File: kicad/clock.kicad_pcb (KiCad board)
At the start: 4 copper layers, 110 x 110 mm, 187 parts, among them J1 USB4160-03-0230-C, J10 Knob: EM14 enc+SW (top face), J11 Radio-off toggle (rear), J12 NeoPixel ext (5V/DATA/GND, po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, J2 PROG, J3 Speaker DMA58-4 (4R), J6 DM3AT-SF-PEJM5, J7 Sensor board (BME688+TSL2591+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, J9 Wake COB 12V (warm+cool), M1 X40.879, Q1 2N7002, Q2 AO3401A, Q3 2N7002, Q4 AO3401A, Q6 AO3400A, Q7 AO3400A, Q8 2N7002, Q9 AO3401A, SW1 RESET, SW2 BOOT, U1 CH224K, U10 LTC4412ES6, U11 TB6612FNG, U12 TB6612FNG, U13 MCP23017, U14 QRE1113GR, U15 SN74AHCT1G125, U16 USBLC6-2SC6, U2 LT3652EMSE, U3 HY2111-GB, U4 AOSD32334C, U5 TPS61023, U6 TLV62569DBVR, U7 TPS55340PWPR, U8 ESP32-S3-WROOM-1-N16R8, U9 TAS5760MDAPR, Y1 32.768kHz

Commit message: Move C238 next to U15 (#9)
The SN74AHCT1G125 buffer that drives the whole SK6812 chain had its bypass
capacitor 50.5 mm away, i.e. no local decoupling at all.

  C238 (76.50, 39.50) -> (26.73, 46.18) rot 180
  pad 1 (+5V) to U15 pin 5 (VCC):  50.50 -> 1.75 mm
  new 0.50 mm B.Cu trace, 2 GND vias 0.62 mm from its return pad
  (nearest GND via was 2.68 mm)

One subtlety worth recording: C238's +5V pad was not a leaf but a JUNCTION
between two collinear B.Cu tracks, (77.28,44.36)->pad and (77.28,33.61)->pad.
Cutting both, as the mover did at first, split +5V into two islands.  Tracks
that share an endpoint stay connected without the pad, so the rule is now to
cut only when the pad holds a single stub, and to leave junctions alone.

DRC 0 errors / 0 warnings / 0 unconnected; review_check.py 11/12, 0 regressions.

Co-Authored-By: Claude Opus 5 <noreply@anthropic.com>
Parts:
- moved C238 50.2 mm to (26.7, 46.2)
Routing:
- net +5V: track 265.3 -> 267.1 mm
- net GND: vias 477 -> 479
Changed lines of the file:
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@@
 	(footprint "Capacitor_SMD:C_0603_1608Metric"
 		(layer "B.Cu")
-		(at 76.5 39.5 180)
+		(at 26.73 46.18 180)
 		(descr "Capacitor SMD 0603 (1608 Metric), square (rectangular) end terminal, IPC-7351 nominal, (Body size source: IPC-SM-782 page 76, https://www.pcb-3d.com/wordpress/wp-content/uploads/ipc-sm-782a_amendment_1_and_2.pdf)")
 		(tags "capacitor")
@@
 	)
 	(via
+		(at 25.879664 46.800443)
+		(size 0.8)
+		(drill 0.4)
+		(layers "F.Cu" "B.Cu")
+		(net "GND")
+	)
+	(via
 		(at 56.925 41.925)
 		(size 0.6)
@@
 	)
 	(via
+		(at 26.58 46.18)
+		(size 0.6)
+		(drill 0.3)
+		(layers "F.Cu" "B.Cu")
+		(net "GND")
+	)
+	(via
 		(at 62.925 71.925)
 		(size 0.6)
@@
 		(layer "B.Cu")
 		(net "+5V")
+	)
+	(segment
+		(start 27.505 46.18)
+		(end 27.48 47.93)
+		(width 0.5)
+		(layer "B.Cu")
+		(net "+5V")

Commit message: Re-place and re-route the 32.768 kHz cluster (#24)
Item 1 of the #24 recommendation.  The load caps were 5.85 mm from Y1 and
their nets wandered 9.1 mm (XTAL_P) and 14.0 mm (XTAL_N) to reach them --
a large loop on MOhm-impedance nodes sitting near the switchers.

  C145 -> (58.90, 18.50)   pad 2 to Y1 pin 2:  5.85 -> 2.60 mm
  C146 -> (56.35, 22.11)   pad 2 to Y1 pin 1:  5.85 -> 1.75 mm
  XTAL_P copper   9.1 -> 5.46 mm   XTAL_N copper  14.0 -> 4.95 mm
  both nets on B.Cu only, 0 vias, as the recommendation asks
  4 GND vias ring the pair (0.62-1.52 mm from their return pads)

This could not be done as two independent part moves: the XTAL traces were
themselves counted as obstacles, yet they existed only to reach the caps'
old position, so nothing would fit next to Y1 until both nets were stripped
first.  It is one delete-place-reroute job.

Two tooling bugs it exposed, both now fixed:
  * courtyard collision was tested on BOUNDING BOXES.  U8's courtyard is a T
    (module body + antenna keep-out) whose bbox spans x[19.95,68.05]
    y[-13.79,27.50] and swallows the whole crystal corner, so every candidate
    near Y1 was rejected.  Now uses the real polygon.
  * a failed candidate restored the footprint ORIGIN to the PAD's coordinates,
    silently shifting both caps by the pad offset.

C145's first slot overlapped a hand-drawn 0.1 mm silk mark at (57.00,16.50)->
(58.50,18.00); C145 was nudged to clear it rather than moving the mark.
Reference fields for Y1/C145/C146/R113 were repositioned into the space the
caps vacated -- they had kept their old offsets and collided.

DRC 0 errors / 0 warnings / 0 unconnected; review_check.py 11/12, 0 regressions.

Co-Authored-By: Claude Opus 5 <noreply@anthropic.com>
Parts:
- moved C145 6.00 mm to (58.9, 18.5)
- moved C146 4.11 mm to (56.4, 22.1)
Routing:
- net Net-(U8-IO16_XTAL_N): track 14.0 -> 4.95 mm
- net Net-(U8-IO15_XTAL_P): track 9.06 -> 5.46 mm
- net GND: vias 479 -> 483
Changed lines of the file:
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@@
 	(footprint "Capacitor_SMD:C_0603_1608Metric"
 		(layer "B.Cu")
-		(at 55.905 26.2 180)
+		(at 56.35 22.115 180)
 		(descr "Capacitor SMD 0603 (1608 Metric), square (rectangular) end terminal, IPC-7351 nominal, (Body size source: IPC-SM-782 page 76, https://www.pcb-3d.com/wordpress/wp-content/uploads/ipc-sm-782a_amendment_1_and_2.pdf)")
 		(tags "capacitor")
 		(property "Reference" "C146"
-			(at -0.095 -1.8 0)
+			(at -0.1 -1.795 0)
 			(layer "B.SilkS")
 			(effects
@@
 		(tags "SMD SMT Crystal")
 		(property "Reference" "Y1"
-			(at 2.775 -0.4 0)
+			(at 6.185 0 0)
 			(layer "B.SilkS")
 			(effects
@@
 	(footprint "Capacitor_SMD:C_0603_1608Metric"
 		(layer "B.Cu")
-		(at 55.905 23.7 180)
+		(at 58.9 18.5 180)
 		(descr "Capacitor SMD 0603 (1608 Metric), square (rectangular) end terminal, IPC-7351 nominal, (Body size source: IPC-SM-782 page 76, https://www.pcb-3d.com/wordpress/wp-content/uploads/ipc-sm-782a_amendment_1_and_2.pdf)")
 		(tags "capacitor")
 		(property "Reference" "C145"
-			(at -2.595 -1.3 0)
+			(at -3.1 0 0)
 			(layer "B.SilkS")
 			(effects
@@
 		(tags "resistor")
 		(property "Reference" "R113"
-			(at -2.1682 -3.315 180)
+			(at -3.0682 0.485 180)
 			(layer "B.SilkS")
 			(effects
@@
 	)
 	(via
+		(at 60.22841 18.209548)
+		(size 0.8)
+		(drill 0.4)
+		(layers "F.Cu" "B.Cu")
+		(net "GND")
+	)
+	(via
 		(at 5.925 47.925)
 		(size 0.6)
@@
 	)
 	(via
+		(at 57.276194 21.354891)
+		(size 0.6)
+		(drill 0.3)
+		(layers "F.Cu" "B.Cu")
+		(net "GND")
+	)
+	(via
 		(at 32.925 38.925)
 		(size 0.6)
@@
 	)
 	(via
+		(at 61.014287 17.770662)
+		(size 0.8)
+		(drill 0.4)
+		(layers "F.Cu" "B.Cu")
+		(net "GND")
+	)
+	(via
 		(at 107.925 23.925)
 		(size 0.6)
@@
 	)
 	(via
+		(at 57.75 22.115)
+		(size 0.8)
+		(drill 0.4)
+		(layers "F.Cu" "B.Cu")
+		(net "GND")
+	)
+	(via
 		(at 26.925 83.925)
 		(size 0.6)
@@
 	)
 	(segment
-		(start 55.13 23.7)
-		(end 54.4496 23.0196)
-		(width 0.25)
-		(layer "B.Cu")
-		(net "Net-(U8-IO15_XTAL_P)")
-	)
-	(segment
-		(start 55.6 17.865)
-		(end 54.4496 17.865)
-		(width 0.25)
-		(layer "B.Cu")
-		(net "Net-(U8-IO15_XTAL_P)")
-	)
-	(segment
-		(start 54.4496 17.865)
-		(end 53.985 17.865)
-		(width 0.25)
-		(layer "B.Cu")
-		(net "Net-(U8-IO15_XTAL_P)")
-	)
-	(segment
-		(start 53.985 17.865)
-		(end 53.75 17.63)
+		(start 55.6 17.86)
+		(end 58.125 18.5)
 		(width 0.25)
 		(layer "B.Cu")
@@
 	(segment
 		(start 52.75 17.63)
-		(end 53.75 17.63)
-		(width 0.25)
-		(layer "B.Cu")
-		(net "Net-(U8-IO15_XTAL_P)")
-	)
-	(segment
-		(start 54.4496 23.0196)
-		(end 54.4496 17.865)
+		(end 55.6 17.865)
 		(width 0.25)
 		(layer "B.Cu")
@@
 	)
 	(segment
-		(start 52.75 18.9)
-		(end 53.75 18.9)
-		(width 0.25)
-		(layer "B.Cu")
-		(net "Net-(U8-IO16_XTAL_N)")
-	)
-	(segment
-		(start 55.8159 21.3309)
-		(end 55.8159 24.1907)
-		(width 0.25)
-		(layer "B.Cu")
-		(net "Net-(U8-IO16_XTAL_N)")
-	)
-	(segment
 		(start 55.6 20.365)
-		(end 55.6 21.115)
-		(width 0.25)
-		(layer "B.Cu")
-		(net "Net-(U8-IO16_XTAL_N)")
-	)
-	(segment
-		(start 55.6 21.115)
-		(end 55.8159 21.3309)
-		(width 0.25)
-		(layer "B.Cu")
-		(net "Net-(U8-IO16_XTAL_N)")
-	)
-	(segment
-		(start 55.5587 24.4479)
-		(end 55.5587 25.7713)
+		(end 55.575 22.115)
 		(width 0.25)
 		(layer "B.Cu")
@@
 	)
 	(segment
-		(start 54.7173 24.4479)
-		(end 53.75 23.4806)
-		(width 0.25)
-		(layer "B.Cu")
-		(net "Net-(U8-IO16_XTAL_N)")
-	)
-	(segment
-		(start 55.5587 25.7713)
-		(end 55.13 26.2)
-		(width 0.25)
-		(layer "B.Cu")
-		(net "Net-(U8-IO16_XTAL_N)")
-	)
-	(segment
-		(start 55.8159 24.1907)
-		(end 55.5587 24.4479)
-		(width 0.25)
-		(layer "B.Cu")
-		(net "Net-(U8-IO16_XTAL_N)")
-	)
-	(segment
-		(start 53.75 23.4806)
-		(end 53.75 18.9)
-		(width 0.25)
-		(layer "B.Cu")
-		(net "Net-(U8-IO16_XTAL_N)")
-	)
-	(segment
-		(start 55.5587 24.4479)
-		(end 54.7173 24.4479)
+		(start 52.75 18.9)
+		(end 55.6 20.365)
 		(width 0.25)
 		(layer "B.Cu")

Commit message: bom: MCU module N16R8 -> ESP32-S3-WROOM-1-N8R8
The 16 MB flash SKU was chosen back when the design carried the Sharp
display; it is also the harder variant to source. N8R8 is the DevKitC-1
stock variant, $6.32 / 1,709 in stock at DigiKey 15295891 (active) vs
$6.76 for the N16R8.

Verified drop-in against the WROOM-1/1U datasheet v1.8:

- Table 3-1 Pin Definitions is a single table for the whole series --
  41 pads, no per-SKU variation -- and the body stays 18.0 x 25.5 x
  3.1 mm, so the RF_Module:ESP32-S3-WROOM-1 land is unchanged.
- Note b reserves IO35/36/37 on any Octal-SPI-PSRAM module (ESP32-S3R8
  or R16V). N8R8 is R8, so the same 3 pads are eaten and the GPIO
  budget stays 32/33.
- R8 ambient range is unchanged at -40 ~ 65 C.
- Only the flash die differs: 16 MB -> 8 MB (Quad SPI).

Schematic/PCB changes are therefore text-only: MPN, Value and
Description on U8. No net, footprint or placement moved; ERC still
reports 0 violations and review_check.py is unchanged at 11/12 (the
U2 thermal-via TODO predates this). PCB copper untouched.

The one real cost is the partition table, reflowed for 8 MB in
FIRMWARE.md: OTA slots 3 M -> 2.5 M each, assets ~9 M -> ~2.7 M, with
coredump moved ahead of the app slots to keep ota_0 64 K-aligned at
0x40000. User tones were already microSD-only.

Also fixes the regen recipe in kicad/README.md, which omitted
stamp_bom.py -- without it build.py drops every BOM field from the
sheet.

Co-Authored-By: Claude Opus 5 <noreply@anthropic.com>
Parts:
- U8: value ESP32-S3-WROOM-1-N16R8 -> ESP32-S3-WROOM-1-N8R8
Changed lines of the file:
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@@
 			)
 		)
-		(property "Value" "ESP32-S3-WROOM-1-N16R8"
+		(property "Value" "ESP32-S3-WROOM-1-N8R8"
 			(at 0 -14.6 0)
 			(unlocked yes)
@@
 			)
 		)
-		(property "Description" "MODULE ESP32-S3 WIFI/BLE 16MB FLASH 8MB PSRAM"
+		(property "Description" "MODULE ESP32-S3 WIFI/BLE 8MB FLASH 8MB PSRAM"
 			(at 0 0 0)
 			(unlocked yes)
@@
 			)
 		)
-		(property "MPN" "ESP32-S3-WROOM-1-N16R8"
+		(property "MPN" "ESP32-S3-WROOM-1-N8R8"
 			(at 0 0 0)
 			(unlocked yes)

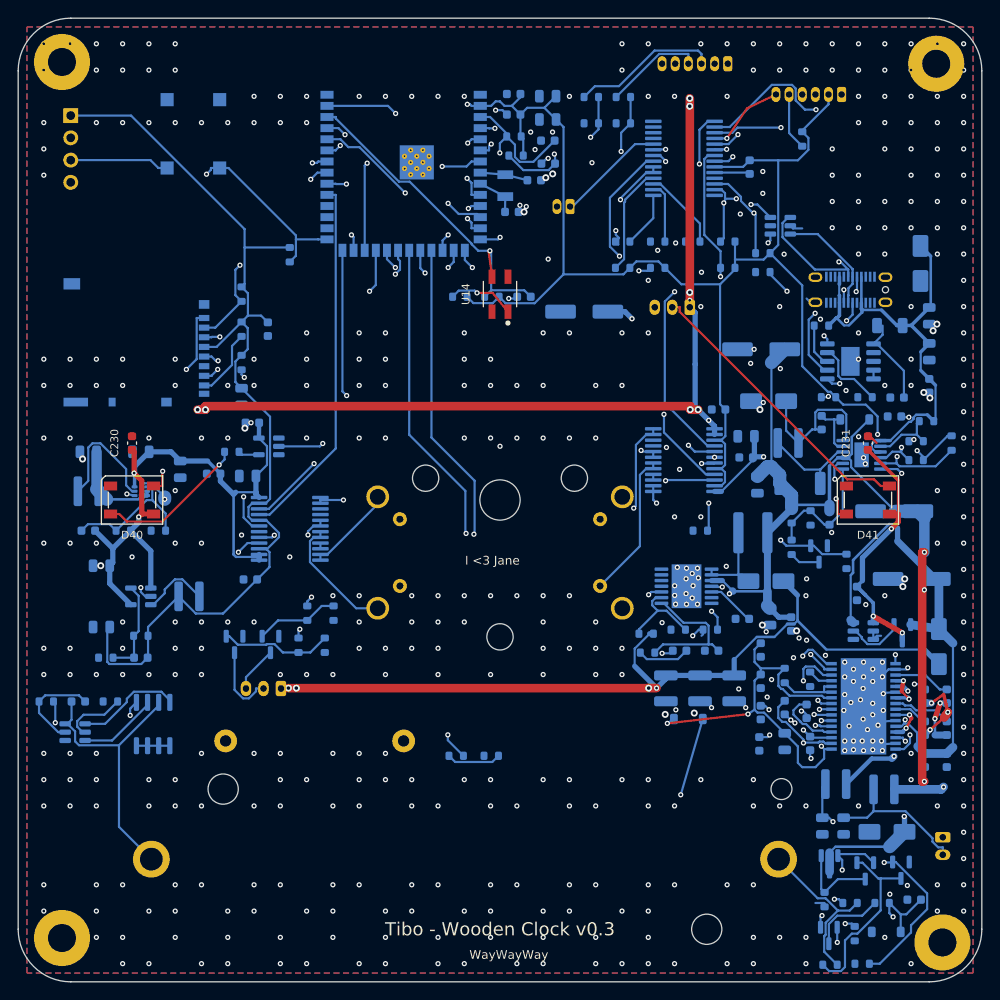
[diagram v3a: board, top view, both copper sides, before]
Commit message: pcb: pre-fab audit — R1 latent open (#26), +3V3 widths (#4), title block
Bundles the hand edits made in pcbnew (Y1 reference reposition, Q2 VBAT
stub re-route) with a pre-fab audit pass over the routed board looking
for defects that kicad-cli drc structurally cannot report.

#26 — R1 pad 2 was hanging on 0.049 mm of copper. A latent open left by
the #13 0603 -> 1206 land swap: the track ended at x = 98.675, dead
centre of the *old* 0603 pad, while the 1206 pad's outer edge sits at
98.600. Only the track's 0.125 mm end cap still overlapped. DRC was
silent because connectivity is a boolean -- any overlap reads as
connected. R1 feeds the CH224K's shunt-regulated VDD, so an open there
means no PD negotiation: no 15 V, no charging, no 12 V rail. Fixed with
one B.Cu segment to the pad centre, lying entirely inside the pad plus
the existing end cap, so no copper exists anywhere it did not already.

Sweeping the whole board for the same class found nothing else: 0 pads
and 0 free track ends now bridge on less than 0.12 mm (was 1 and 1,
both R1).

#4 — +3V3 widened in place. It was never in the POWER net class, so
a20faef skipped it and all 423 mm was still 0.25 mm, making it the
highest-resistance rail on the board. Width-only, no endpoint or part
moves, capped 0.80 mm outer / 0.60 mm inner:

    L3 -> U8 ESP32 3V3   258 -> 169 mOhm
    L3 -> U9 DVDD/AVDD   569/512 -> 393/346
    L3 -> U13 / U11 / J7 405/388/413 -> 273/270/285
    net total            837 -> 555 mOhm  (-34 %)

97 of 164 segments. Only the MCU figure has real consequences: DC droop
at a 500 mA Wi-Fi TX peak goes 129 -> 85 mV against 300 mV of margin to
the 3.0 V floor. Widening an inner-layer trace does not worsen #18 --
a slot's return-path cost is set by its length, not its width.

The pass tripped U9's local 0.2 mm clearance override (twice the board
rule, the same trap f480ced hit): 3 clearance errors plus a starved
thermal on C161. The 12 +3V3 segments within 2.5 mm of a U9 pad, and 2
near C161's GND pa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
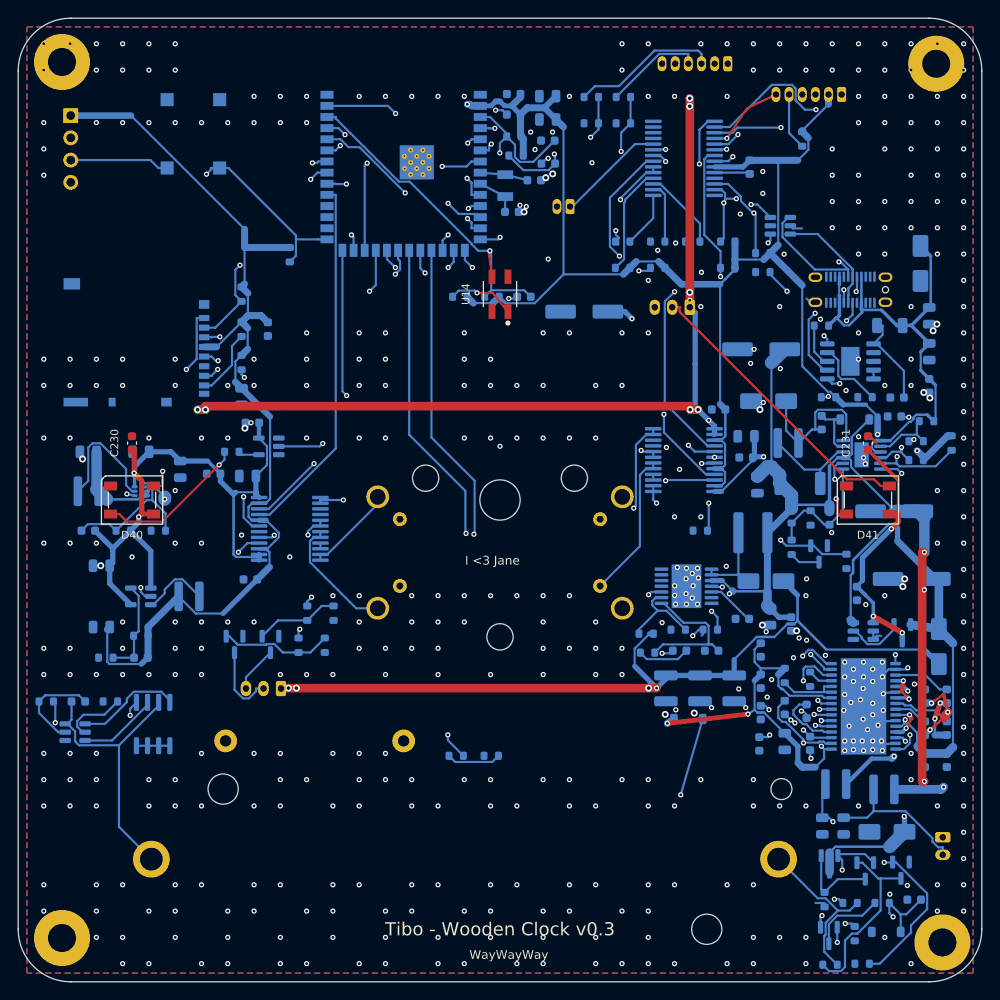
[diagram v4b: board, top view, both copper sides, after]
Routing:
- net Net-(U1-VDD): track 10.2 -> 10.8 mm
